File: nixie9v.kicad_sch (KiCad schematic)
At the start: 21 parts

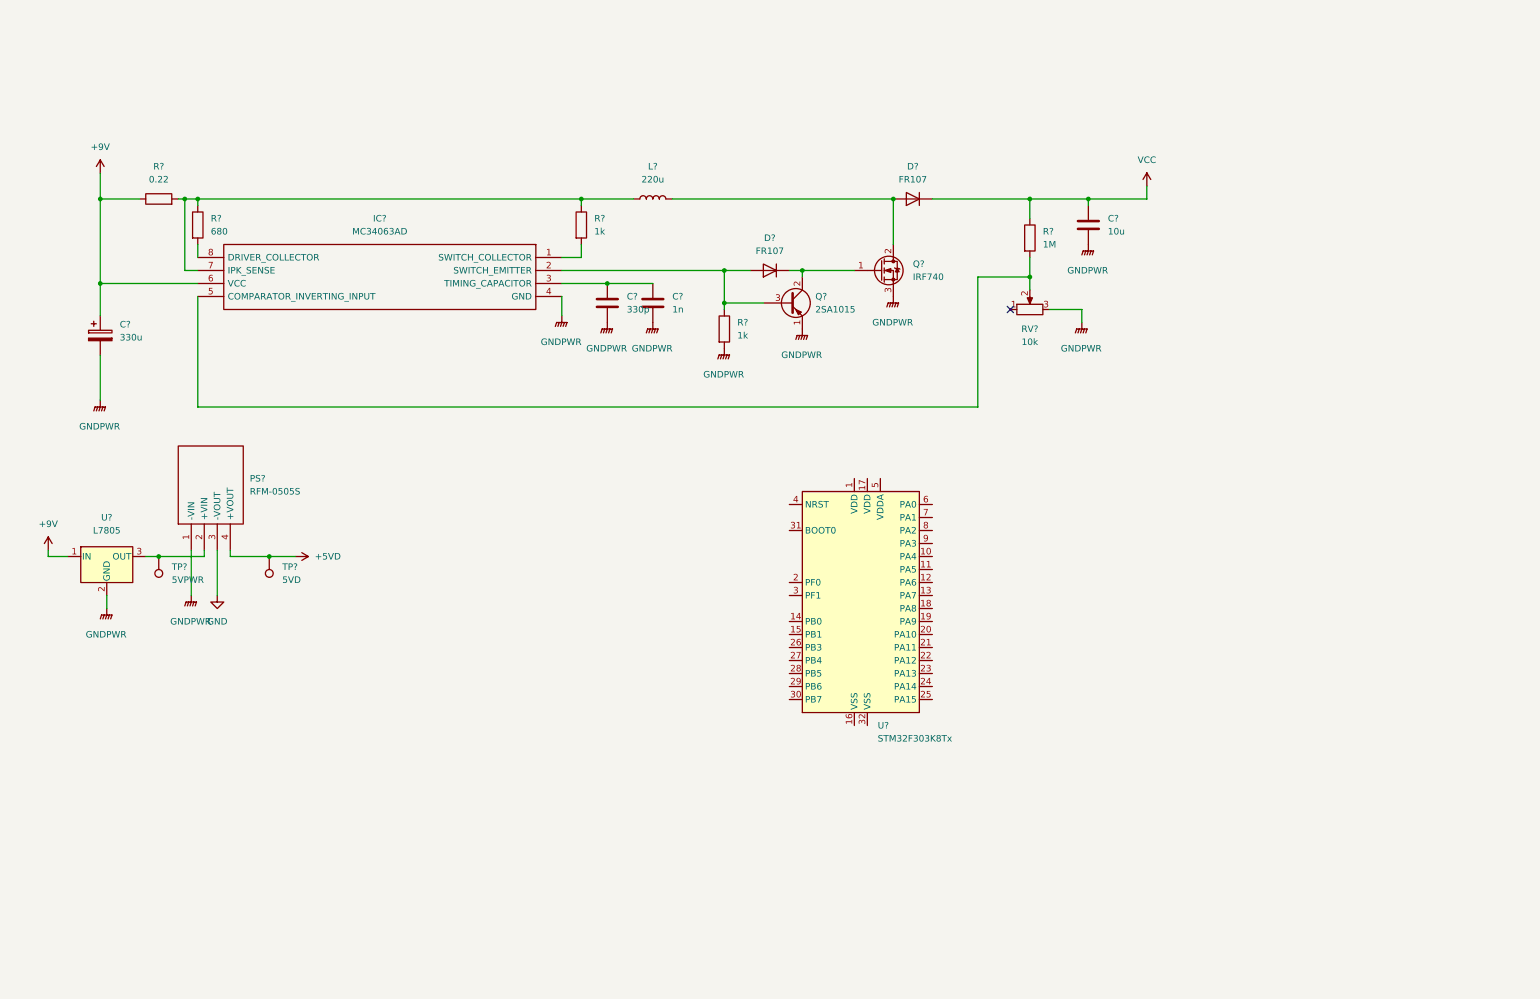
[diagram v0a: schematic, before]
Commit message: add mcu
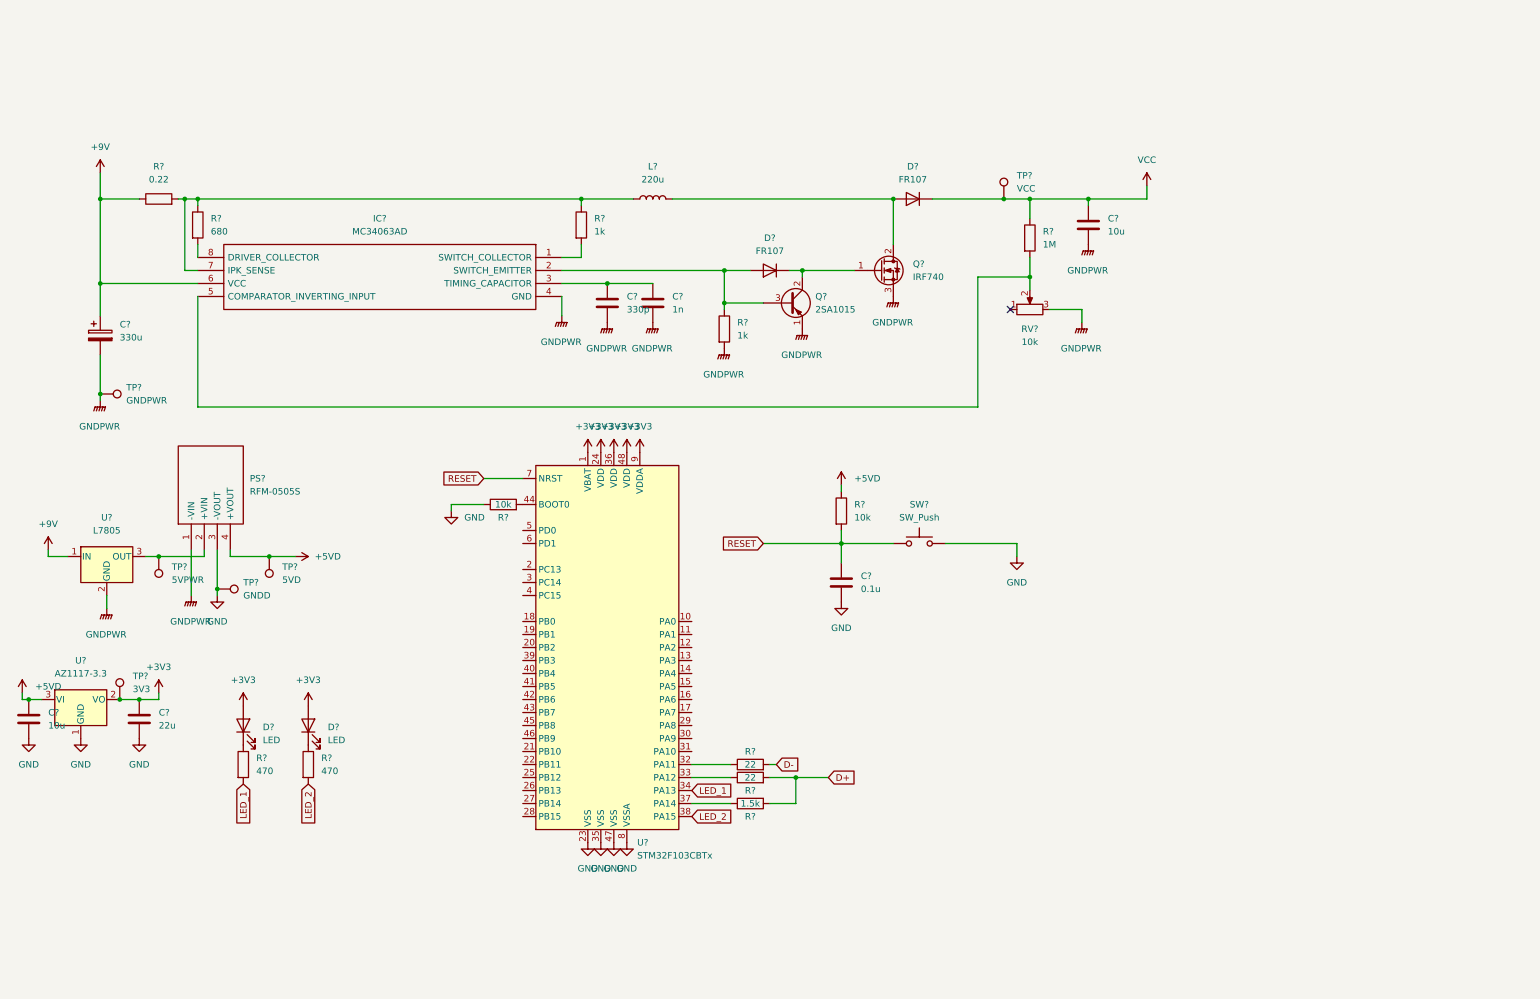
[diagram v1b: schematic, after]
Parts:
- removed U?: STM32F303K8Tx, Package_QFP:LQFP-32_7x7mm_P0.8mm, symbol MCU_ST_STM32F3:STM32F303K8Tx
- added C?: 0.1u, symbol Device:C
- added C?: 22u, symbol Device:C
- added C?: 10u, symbol Device:C
- added D? (x2): LED, symbol Device:LED
- added R? (x2): 470, symbol Device:R
- added R? (x2): 22, symbol Device:R
- added R?: 1.5k, symbol Device:R
- added R? (x2): 10k, symbol Device:R
- added SW?: SW_Push, symbol Switch:SW_Push
- added TP?: VCC, symbol Connector:TestPoint
- added TP?: GNDD, symbol Connector:TestPoint
- added TP?: 3V3, symbol Connector:TestPoint
- added TP?: GNDPWR, symbol Connector:TestPoint
- added U?: STM32F103CBTx, Package_QFP:LQFP-48_7x7mm_P0.5mm, symbol MCU_ST_STM32F1:STM32F103CBTx
- added U?: AZ1117-3.3, symbol Regulator_Linear:AZ1117-3.3
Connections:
- net +5VD: now also C?.1, R?.1, U?.3 (VI)
- net GND: now also C?.2, C?.2, C?.2, R?.1, SW?.2, TP?.1, U?.1 (GND), U?.23 (VSS), U?.35 (VSS), U?.47 (VSS), U?.8 (VSSA)
- net GNDPWR: now also TP?.1
- net VCC: now also TP?.1
- new net: D?.1 (K), R?.1 (x2)
- new net: R?.1, U?.32 (PA11)
- new net: R?.1, U?.33 (PA12)
- new net: R?.1, U?.37 (PA14)
- new net: R?.2, U?.44 (BOOT0)
- new net +3V3: C?.1, D?.2 (A), D?.2 (A), TP?.1, U?.1 (VBAT), U?.2 (VO), U?.24 (VDD), U?.36 (VDD), U?.48 (VDD), U?.9 (VDDA)
- new net D+: R?.2, R?.2
- new net D-: R?.2
- new net LED_1: R?.2, U?.34 (PA13)
- new net LED_2: R?.2, U?.38 (PA15)
- new net RESET: C?.1, R?.2, SW?.1, U?.7 (NRST)

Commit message: sch accomplished
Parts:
- removed R?: 1.5k, symbol Device:R
- added C12, C5, C7: 0.1u, symbol Device:C
- added C4, C6: 10p, symbol Device:C
- added D2: LED, symbol Device:LED
- added J1: USB_B_Mini, symbol Connector:USB_B_Mini
- added J2: UART, symbol Connector_Generic:Conn_01x04
- added J3: STLINK, symbol Connector_Generic:Conn_01x04
- added R14: 10k, symbol Device:R
- added R4: 470, symbol Device:R
- added R9: 1.5k, symbol Device:R
- added SW1: SW_SPST, symbol Switch:SW_SPST
- added SW3: RESET, symbol Switch:SW_Push
- added Y1: Crystal, symbol Device:Crystal
- IC1: renamed from IC?; footprint SOIC127P600X175-8N -> MC34063AD:SOIC127P600X175-8N
- PS1: renamed from PS?; footprint RFM0505S -> RFM-0505S:RFM0505S
- SW2: renamed from SW?; value SW_Push -> RESET
- gave numbers to parts that had none: 35
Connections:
- net +3V3: now also C5.1, C7.1, D2.2 (A), J2.4 (Pin_4)
- net +5VD: now also J1.1 (VBUS), R14.1, SW1.2 (B); no longer PS1.4 (+VOUT), TP5.1
- net D+: now also J1.3 (D+), R9.2
- net D-: now also J1.2 (D-)
- net GND: now also C12.2, C4.2, C5.2, C6.2, C7.2, J1.4 (ID), J1.5 (GND), J1.6 (Shield), J2.3 (Pin_3), J3.3 (Pin_3), SW3.2
- net LED_1: now also U3.18 (PB0); no longer U3.34 (PA13)
- net LED_2: now also U3.19 (PB1); no longer U3.38 (PA15)
- net UART_TX: now reaches U3.17 (PA7)
- net UART_TX: now also J2.2 (Pin_2)
- net USER_SW: now reaches U3.2 (PC13)
- net USER_SW: now also C12.1, R14.2, SW3.1
- net LED_3: now reaches U3.20 (PB2)
- net LED_3: now also R4.2
- net D: now reaches U3.21 (PB10)
- net UART_RX: now reaches U3.29 (PA8)
- net UART_RX: now also J2.1 (Pin_1)
- net SWCLK: now reaches U3.37 (PA14)
- net SWCLK: now also J3.1 (Pin_1)
- net Tube_1: now reaches U3.39 (PB3)
- net Tube_2: now reaches U3.40 (PB4)
- net Tube_3: now reaches U3.41 (PB5)
- net Tube_4: now reaches U3.42 (PB6)
- net A: now reaches U3.43 (PB7)
- net B: now reaches U3.45 (PB8)
- net C: now reaches U3.46 (PB9)
- net at U3.5 (PD0): now also C4.1, Y1.1
- net at U3.6 (PD1): now also C6.1, Y1.2
- net +5VA: now reaches PS1.2 (+VIN), TP3.1, U1.3 (OUT)
- net RESET renamed NRST
- net NRST: now also J3.4 (Pin_4)
- new net: R9.1, U3.38 (PA15)
- new net: D2.1 (K), R4.1
- new net: PS1.4 (+VOUT), SW1.1 (A), TP5.1
- new net SWDIO: J3.2 (Pin_2), U3.34 (PA13)
- no-connect marks 1 -> 17
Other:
- added sheet Control_circuit (untitled.kicad_sch)
- moved on the sheet: PS1, TP3, TP4, TP5, U1

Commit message: add switch and footprint mapping in the middle
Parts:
- removed J1: USB_B_Mini, symbol Connector:USB_B_Mini
- added J1: USB_B_Micro, Connector_USB:USB_Micro-B_Wuerth_629105150521_CircularHoles, symbol Connector:USB_B_Micro
- added J6: Barrel_Jack, Connector_BarrelJack:BarrelJack_Horizontal, symbol Connector:Barrel_Jack
- added Q3, Q4: IRLML6402, Package_TO_SOT_SMD:SOT-23, symbol Transistor_FET:IRLML6402
- added R23, R24: 10k, Resistor_SMD:R_0603_1608Metric_Pad0.98x0.95mm_HandSolder, symbol Device:R
- added SW4: PWR_SW, symbol Switch:SW_SPDT
- C1, C10, C12, C2, C3, C4, C5, C6, C7, C8, C9: footprint (none) -> Capacitor_SMD:C_0603_1608Metric_Pad1.08x0.95mm_HandSolder
- C11: value 10u -> 10u 300V; footprint (none) -> Capacitor_SMD:C_0603_1608Metric_Pad1.08x0.95mm_HandSolder
- D1, D2, D3: footprint (none) -> LED_SMD:LED_0603_1608Metric_Pad1.05x0.95mm_HandSolder
- J2, J3: footprint (none) -> Connector_JST:JST_SH_BM04B-SRSS-TB_1x04-1MP_P1.00mm_Vertical
- R1: value 0.22 -> 0.22 5W
- R10, R11, R12, R13, R14, R2, R3, R4, R5, R6, R7, R8, R9, RV1: footprint (none) -> Resistor_SMD:R_0603_1608Metric_Pad0.98x0.95mm_HandSolder
- SW1: value SW_SPST -> Jumper; footprint (none) -> Connector_PinHeader_2.54mm:PinHeader_1x02_P2.54mm_Vertical
- SW2: footprint (none) -> Button_Switch_SMD:SW_SPST_EVQP2
- SW3: value RESET -> USER_SW; footprint (none) -> Button_Switch_SMD:SW_SPST_EVQP2
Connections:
- net +5VD: now also J1.1 (VBUS), Q3.3 (D); no longer SW1.2 (B)
- net +9V: now also J6.1, Q4.2 (S), R24.2; no longer C2.1, IC1.6 (VCC), R1.1
- net D+: now also J1.3 (D+)
- net D-: now also J1.2 (D-)
- net GND: now also SW1.2 (B), J1.4 (ID), J1.5 (GND), J1.6 (Shield), SW4.1 (A)
- net GNDPWR: now also J6.2
- net at PS1.4 (+VOUT), TP5.1: now also Q3.2 (S), R23.1; no longer SW1.1 (A)
- new net: C2.1, IC1.6 (VCC), Q4.3 (D), R1.1
- new net: Q3.1 (G), R23.2, SW1.1 (A)
- new net: Q4.1 (G), R24.1, SW4.2 (B)
- no-connect marks 17 -> 18

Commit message: schema finished
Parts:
- removed C11: 10u 300V, Capacitor_SMD:C_0603_1608Metric_Pad1.08x0.95mm_HandSolder, symbol Device:C
- added C15: 10u, Capacitor_THT:CP_Radial_D10.0mm_P3.50mm, symbol Device:C_Polarized
- added C17, C18, C5, C7: 0.1u, Capacitor_SMD:C_0603_1608Metric_Pad1.08x0.95mm_HandSolder, symbol Device:C
- added C3, C6: 10u, Capacitor_SMD:C_0603_1608Metric_Pad1.08x0.95mm_HandSolder, symbol Device:C
- added R17, R18: 10k, Resistor_SMD:R_0603_1608Metric_Pad0.98x0.95mm_HandSolder, symbol Device:R
- added SW5: USER_SW2, Button_Switch_SMD:SW_SPST_EVQP2, symbol Switch:SW_Push
- added SW6: USER_SW3, Button_Switch_SMD:SW_SPST_EVQP2, symbol Switch:SW_Push
- C2: footprint Capacitor_SMD:C_0603_1608Metric_Pad1.08x0.95mm_HandSolder -> Capacitor_THT:CP_Radial_D10.0mm_P3.50mm
- D4, D5: footprint (none) -> Diode_SMD:D_SMF
- L1: footprint (none) -> Inductor_THT:L_Toroid_Horizontal_D24.1mm_P21.80mm_Bourns_2200
- Q3: renamed from Q1; footprint (none) -> Package_TO_SOT_THT:TO-92
- R2: renamed from R1; footprint (none) -> SMW5R22JT:RESM17073X710N
- RV1: footprint Resistor_SMD:R_0603_1608Metric_Pad0.98x0.95mm_HandSolder -> 3362P:3362P_1
- SW1: renamed from SW4; footprint (none) -> Connector_PinHeader_2.54mm:PinHeader_1x03_P2.54mm_Vertical
- SW4: renamed from SW3; value USER_SW -> USER_SW1
- TP1, TP2, TP3, TP4, TP5, TP6: footprint (none) -> TestPoint:TestPoint_THTPad_D2.5mm_Drill1.2mm
- U1: footprint (none) -> Package_TO_SOT_THT:TO-220-3_Vertical
- U2: footprint (none) -> Package_TO_SOT_SMD:SOT-223-3_TabPin2
- Y1: footprint (none) -> Crystal:Crystal_SMD_SeikoEpson_MA505-2Pin_12.7x5.1mm_HandSoldering
- renumbered C6 to C10, C7 to C11, C8 to C12, C9 to C13, C10 to C14, C12 to C16, C3 to C4, C4 to C8, C5 to C9, J6 to J1, J1 to J2, J2 to J3, J3 to J4, Q4 to Q1, Q3 to Q2, Q2 to Q4, R24 to R1, R8 to R10, R9 to R11, R10 to R12, R11 to R13, R12 to R14, R13 to R15, R14 to R16, R2 to R3, R3 to R4, R4 to R5, R23 to R6, R5 to R7, R6 to R8, R7 to R9, SW1 to SW2, SW2 to SW3
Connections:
- net +5VA: now also C3.1, C5.1
- net +5VD: now also R17.1, R18.1
- net GND: now also C17.2, C18.2, SW5.2, SW6.2
- net GNDPWR: now also C15.2, C3.2, C5.2, C6.2, C7.2
- net VCC: now also C15.1
- net USER_SW2: now reaches U3.3 (PC14)
- net USER_SW2: now also C17.1, R17.2, SW5.1
- net USER_SW3: now reaches U3.4 (PC15)
- net USER_SW3: now also C18.1, R18.2, SW6.1
- net at PS1.4 (+VOUT), Q2.2 (S), R6.1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: now also C6.1, C7.1
- net USER_SW renamed USER_SW1
- no-connect marks 18 -> 16

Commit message: upperside
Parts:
- D4, D5: footprint Diode_SMD:D_SMF -> Diode_THT:D_DO-41_SOD81_P7.62mm_Horizontal
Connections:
- net +3V3: now also R14.1, R16.1, R17.1, R18.1
- net +5VD: no longer R14.1, R16.1, R17.1, R18.1
- net GND: now also C6.2, C7.2; no longer SW1.1 (A)
- net GNDPWR: now also SW1.1 (A); no longer C6.2, C7.2

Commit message: fix Q3 orietention
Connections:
- net GNDPWR: now also Q3.2 (C); no longer Q3.1 (E)
- net at D4.1 (K), Q4.1 (G): now also Q3.1 (E); no longer Q3.2 (C)
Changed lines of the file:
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@@
     (pin "1")
   )
-  (symbol (lib_id "Device:Q_PNP_ECB") (at 166.37 69.85 0) (unit 1)
+  (symbol (lib_id "Device:Q_PNP_ECB") (at 166.37 69.85 0) (mirror x) (unit 1)
     (in_bom yes) (on_board yes) (fields_autoplaced)
     (property "Reference" "Q3" (id 0) (at 171.45 68.5799 0)
@@
       (effects (font (size 1.27 1.27)) (justify left))
     )
-    (property "Footprint" "Package_TO_SOT_THT:TO-92" (id 2) (at 171.45 67.31 0)
+    (property "Footprint" "Package_TO_SOT_THT:TO-92" (id 2) (at 171.45 72.39 0)
       (effects (font (size 1.27 1.27)) hide)
     )
